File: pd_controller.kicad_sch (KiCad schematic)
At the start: 28 parts, among them Q1 IRF9358TRPBF, Q2 BSL308PEH6327XTSA1, U2 CYPD3177-24LQXQT

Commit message: started routing
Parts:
- TP10, TP11, TP12, TP13: footprint TestPoint:TestPoint_Pad_D2.5mm -> TestPoint:TestPoint_Plated_Hole_D3.0mm
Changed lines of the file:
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@@
 			)
 		)
-		(property "Footprint" "TestPoint:TestPoint_Pad_D2.5mm"
+		(property "Footprint" "TestPoint:TestPoint_Plated_Hole_D3.0mm"
 			(at 93.98 125.73 0)
 			(effects
@@
 			)
 		)
-		(property "Footprint" "TestPoint:TestPoint_Pad_D2.5mm"
+		(property "Footprint" "TestPoint:TestPoint_Plated_Hole_D3.0mm"
 			(at 68.58 125.73 0)
 			(effects
@@
 			)
 		)
-		(property "Footprint" "TestPoint:TestPoint_Pad_D2.5mm"
+		(property "Footprint" "TestPoint:TestPoint_Plated_Hole_D3.0mm"
 			(at 119.38 125.73 0)
 			(effects
@@
 			)
 		)
-		(property "Footprint" "TestPoint:TestPoint_Pad_D2.5mm"
+		(property "Footprint" "TestPoint:TestPoint_Plated_Hole_D3.0mm"
 			(at 48.26 125.73 0)
 			(effects

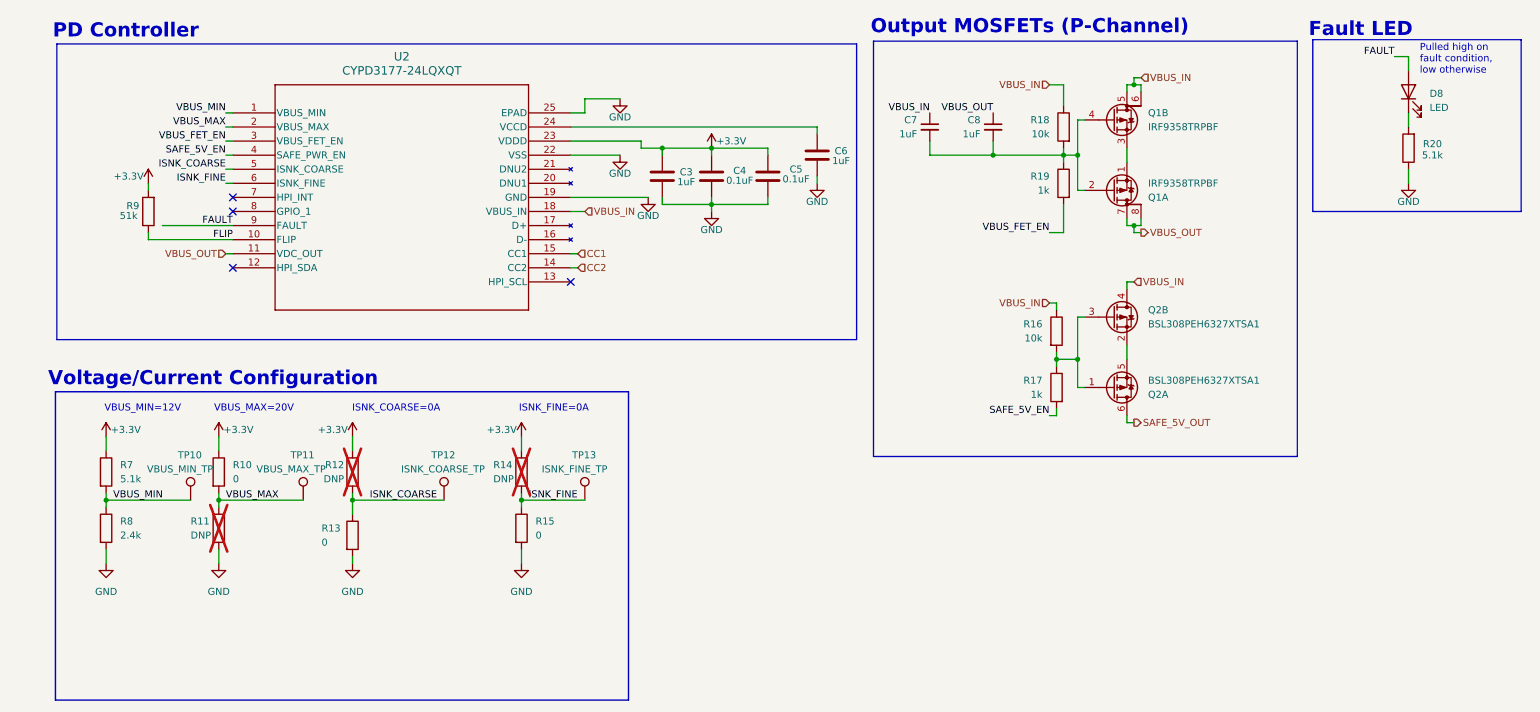
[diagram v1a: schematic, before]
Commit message: redid cypd layout, halfway through 12v buck layout
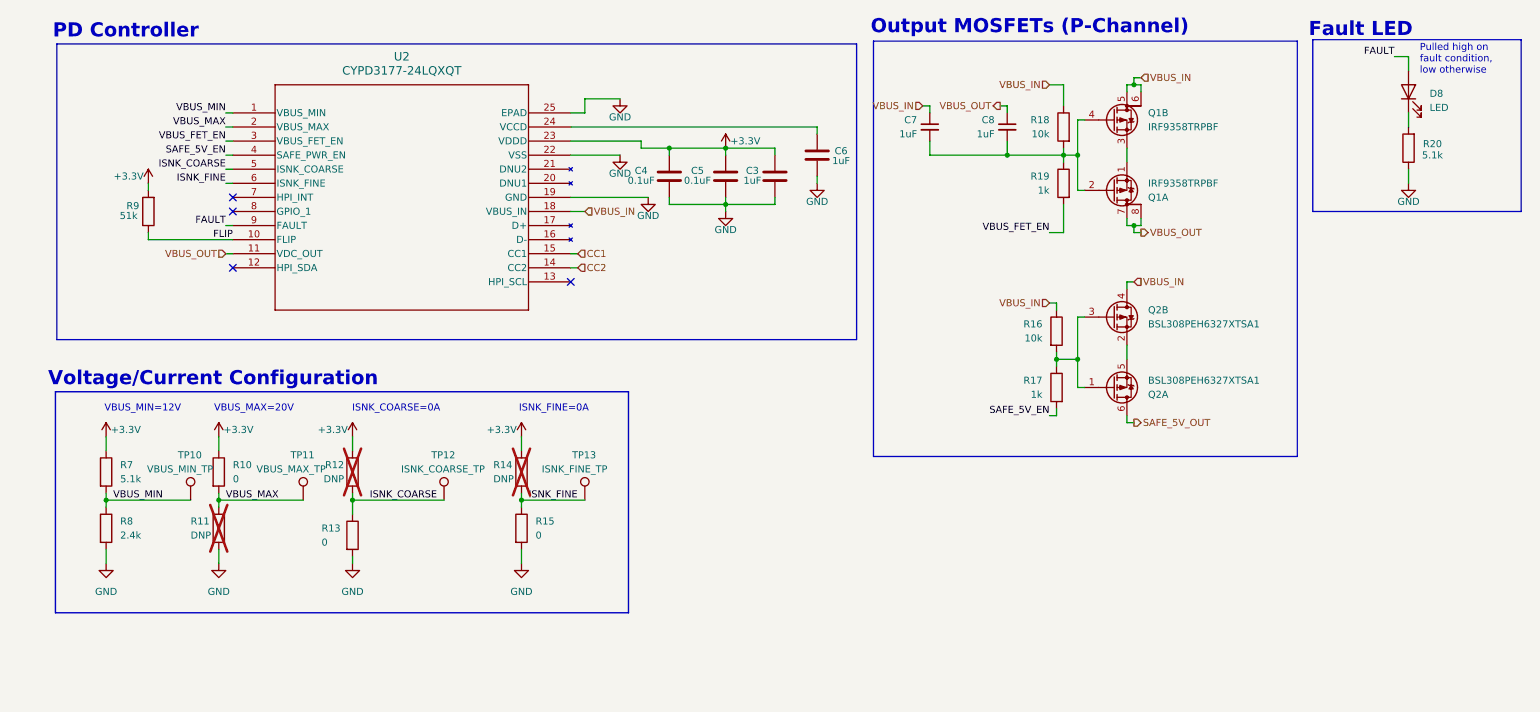
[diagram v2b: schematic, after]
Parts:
- TP10, TP11, TP12, TP13: footprint TestPoint:TestPoint_Plated_Hole_D3.0mm -> TestPoint:TestPoint_THTPad_1.0x1.0mm_Drill0.5mm
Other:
- moved on the sheet: C3, C4, C5, C8

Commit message: addressed some review comments from my 🐐 champers fu
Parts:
- removed TP10: VBUS_MIN_TP, TestPoint:TestPoint_THTPad_1.0x1.0mm_Drill0.5mm, symbol Connector:TestPoint
- removed TP11: VBUS_MAX_TP, TestPoint:TestPoint_THTPad_1.0x1.0mm_Drill0.5mm, symbol Connector:TestPoint
- removed TP12: ISNK_COARSE_TP, TestPoint:TestPoint_THTPad_1.0x1.0mm_Drill0.5mm, symbol Connector:TestPoint
- removed TP13: ISNK_FINE_TP, TestPoint:TestPoint_THTPad_1.0x1.0mm_Drill0.5mm, symbol Connector:TestPoint

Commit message: ready for review 👍🏾
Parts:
- Q1: footprint UTSVT_ICs:SO8_IRF9358TRPBF_INF -> Package_SO:SO-8_3.9x4.9mm_P1.27mm
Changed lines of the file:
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@@
 			)
 		)
-		(property "Footprint" "UTSVT_ICs:SO8_IRF9358TRPBF_INF"
+		(property "Footprint" "Package_SO:SO-8_3.9x4.9mm_P1.27mm"
 			(at 210.82 57.15 0)
 			(effects
@@
 			)
 		)
-		(property "Footprint" "UTSVT_ICs:SO8_IRF9358TRPBF_INF"
+		(property "Footprint" "Package_SO:SO-8_3.9x4.9mm_P1.27mm"
 			(at 210.82 69.85 0)
 			(effects

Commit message: i am jesus christ in the flesh.
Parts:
- C3, C6, C7, C8: Mouser Part Number C0805C105K5PACTU -> (none); P/N (none) -> C0805C105K5PACTU
- C4, C5: Mouser Part Number C0805C104M5RACTU -> (none); P/N (none) -> C0805C104M5RACTU
- D8: Mouser Part Number 604-APTD2012LCGCK -> (none); P/N (none) -> APTD2012LCGCK
- Q1: Mouser Part Number IRF9358TRPBF -> (none); P/N (none) -> IRF9358TRPBF
- Q2: Mouser Part Number BSL308PEH6327XTSA1 -> (none); P/N (none) -> BSL308PEH6327XTSA1
- R16, R18: Mouser Part Number CRCW080510K0FKEAC -> (none); P/N (none) -> CRCW080510K0FKEAC
- R17, R19: Mouser Part Number CRCW08051K00FKEAC -> (none); P/N (none) -> CRCW08051K00FKEAC
- R20, R7: Mouser Part Number CRCW08055K10FKEAC -> (none); P/N (none) -> CRCW08055K10FKEAC
- R8: Mouser Part Number CRCW08052K40FKEAC -> (none); P/N (none) -> CRCW08052K40JNEA
- R9: Mouser Part Number CRCW080551K0FKEAC -> (none); P/N (none) -> CRCW080551K0FKEAC
- U2: Mouser Part Number 727-CYPD3177-24LQXQT -> (none); P/N (none) -> CYPD3177-24LQXQT
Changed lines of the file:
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@@
 			)
 		)
-		(property "Mouser Part Number" "BSL308PEH6327XTSA1"
+		(property "Mouser Part Number" ""
+			(at 209.55 105.41 0)
+			(effects
+				(font
+					(size 1.27 1.27)
+				)
+				(hide yes)
+			)
+		)
+		(property "P/N" "BSL308PEH6327XTSA1"
 			(at 209.55 105.41 0)
 			(effects
@@
 			)
 		)
-		(property "Mouser Part Number" "CRCW080510K0FKEAC "
+		(property "Mouser Part Number" ""
 			(at 200.66 58.42 0)
 			(effects
@@
 			)
 		)
+		(property "P/N" "CRCW080510K0FKEAC"
+			(at 200.66 58.42 0)
+			(effects
+				(font
+					(size 1.27 1.27)
+				)
+				(hide yes)
+			)
+		)
 		(pin "1"
 		)
@@
 			)
 		)
-		(property "Mouser Part Number" "727-CYPD3177-24LQXQT"
+		(property "Mouser Part Number" ""
 			(at 50.8 55.88 0)
 			(effects
@@
 			)
 		)
+		(property "P/N" "CYPD3177-24LQXQT"
+			(at 50.8 55.88 0)
+			(effects
+				(font
+					(size 1.27 1.27)
+				)
+				(hide yes)
+			)
+		)
 		(pin "1"
 		)
@@
 			)
 		)
-		(property "Mouser Part Number" "BSL308PEH6327XTSA1"
+		(property "Mouser Part Number" ""
+			(at 209.55 92.71 0)
+			(effects
+				(font
+					(size 1.27 1.27)
+				)
+				(hide yes)
+			)
+		)
+		(property "P/N" "BSL308PEH6327XTSA1"
 			(at 209.55 92.71 0)
 			(effects
@@
 			)
 		)
-		(property "Mouser Part Number" "604-APTD2012LCGCK"
+		(property "Mouser Part Number" ""
 			(at 262.89 52.07 0)
 			(effects
@@
 			)
 		)
+		(property "P/N" "APTD2012LCGCK"
+			(at 262.89 52.07 0)
+			(effects
+				(font
+					(size 1.27 1.27)
+				)
+				(hide yes)
+			)
+		)
 		(pin "2"
 		)
@@
 			)
 		)
-		(property "Mouser Part Number" "C0805C105K5PACTU"
+		(property "Mouser Part Number" ""
 			(at 176.53 58.42 0)
 			(effects
@@
 			)
 		)
+		(property "P/N" "C0805C105K5PACTU"
+			(at 176.53 58.42 0)
+			(effects
+				(font
+					(size 1.27 1.27)
+				)
+				(hide yes)
+			)
+		)
 		(pin "1"
 		)
@@
 			)
 		)
-		(property "Mouser Part Number" "C0805C105K5PACTU"
+		(property "Mouser Part Number" ""
 			(at 156.21 63.5 0)
 			(effects
@@
 			)
 		)
+		(property "P/N" "C0805C105K5PACTU"
+			(at 156.21 63.5 0)
+			(effects
+				(font
+					(size 1.27 1.27)
+				)
+				(hide yes)
+			)
+		)
 		(pin "1"
 		)
@@
 			)
 		)
-		(property "Mouser Part Number" "C0805C105K5PACTU"
+		(property "Mouser Part Number" ""
 			(at 148.59 67.31 0)
 			(effects
@@
 			)
 		)
+		(property "P/N" "C0805C105K5PACTU"
+			(at 148.59 67.31 0)
+			(effects
+				(font
+					(size 1.27 1.27)
+				)
+				(hide yes)
+			)
+		)
 		(pin "1"
 		)
@@
 			)
 		)
-		(property "Mouser Part Number" "CRCW08052K40FKEAC"
+		(property "Mouser Part Number" ""
 			(at 27.94 130.81 0)
 			(effects
@@
 			)
 		)
+		(property "P/N" "CRCW08052K40JNEA"
+			(at 27.94 130.81 0)
+			(effects
+				(font
+					(size 1.27 1.27)
+				)
+				(hide yes)
+			)
+		)
 		(pin "2"
 		)
@@
 			)
 		)
-		(property "Mouser Part Number" "CRCW08055K10FKEAC "
+		(property "Mouser Part Number" ""
 			(at 27.94 120.65 0)
 			(effects
@@
 			)
 		)
+		(property "P/N" "CRCW08055K10FKEAC "
+			(at 27.94 120.65 0)
+			(effects
+				(font
+					(size 1.27 1.27)
+				)
+				(hide yes)
+			)
+		)
 		(pin "2"
 		)
@@
 			)
 		)
-		(property "Mouser Part Number" "CRCW080510K0FKEAC "
+		(property "Mouser Part Number" ""
 			(at 199.39 95.25 0)
 			(effects
@@
 			)
 		)
+		(property "P/N" "CRCW080510K0FKEAC"
+			(at 199.39 95.25 0)
+			(effects
+				(font
+					(size 1.27 1.27)
+				)
+				(hide yes)
+			)
+		)
 		(pin "1"
 		)
@@
 			)
 		)
-		(property "Mouser Part Number" "C0805C105K5PACTU"
+		(property "Mouser Part Number" ""
 			(at 190.5 58.42 0)
 			(effects
@@
 			)
 		)
+		(property "P/N" "C0805C105K5PACTU"
+			(at 190.5 58.42 0)
+			(effects
+				(font
+					(size 1.27 1.27)
+				)
+				(hide yes)
+			)
+		)
 		(pin "1"
 		)
@@
 			)
 		)
-		(property "Mouser Part Number" "IRF9358TRPBF"
+		(property "Mouser Part Number" ""
+			(at 209.55 57.15 0)
+			(effects
+				(font
+					(size 1.27 1.27)
+				)
+				(hide yes)
+			)
+		)
+		(property "P/N" "IRF9358TRPBF"
 			(at 209.55 57.15 0)
 			(effects
@@
 			)
 		)
-		(property "Mouser Part Number" "C0805C104M5RACTU"
+		(property "Mouser Part Number" ""
 			(at 139.7 67.31 0)
 			(effects
@@
 			)
 		)
+		(property "P/N" "C0805C104M5RACTU"
+			(at 139.7 67.31 0)
+			(effects
+				(font
+					(size 1.27 1.27)
+				)
+				(hide yes)
+			)
+		)
 		(pin "1"
 		)
@@
 			)
 		)
-		(property "Mouser Part Number" "C0805C104M5RACTU"
+		(property "Mouser Part Number" ""
 			(at 129.54 67.31 0)
 			(effects
@@
 			)
 		)
+		(property "P/N" "C0805C104M5RACTU"
+			(at 129.54 67.31 0)
+			(effects
+				(font
+					(size 1.27 1.27)
+				)
+				(hide yes)
+			)
+		)
 		(pin "1"
 		)
@@
 			)
 		)
-		(property "Mouser Part Number" "CRCW08051K00FKEAC"
+		(property "Mouser Part Number" ""
 			(at 200.66 68.58 0)
 			(effects
@@
 			)
 		)
+		(property "P/N" "CRCW08051K00FKEAC"
+			(at 200.66 68.58 0)
+			(effects
+				(font
+					(size 1.27 1.27)
+				)
+				(hide yes)
+			)
+		)
 		(pin "1"
 		)
@@
 			)
 		)
-		(property "Mouser Part Number" "CRCW08051K00FKEAC"
+		(property "Mouser Part Number" ""
 			(at 199.39 105.41 0)
 			(effects
@@
 			)
 		)
+		(property "P/N" "CRCW08051K00FKEAC"
+			(at 199.39 105.41 0)
+			(effects
+				(font
+					(size 1.27 1.27)
+				)
+				(hide yes)
+			)
+		)
 		(pin "1"
 		)
@@
 			)
 		)
-		(property "Mouser Part Number" "CRCW080551K0FKEAC"
+		(property "Mouser Part Number" ""
 			(at 35.56 73.66 0)
 			(effects
@@
 			)
 		)
+		(property "P/N" "CRCW080551K0FKEAC"
+			(at 35.56 73.66 0)
+			(effects
+				(font
+					(size 1.27 1.27)
+				)
+				(hide yes)
+			)
+		)
 		(pin "2"
 		)
@@
 			)
 		)
-		(property "Mouser Part Number" "CRCW08055K10FKEAC "
+		(property "Mouser Part Number" ""
 			(at 262.89 62.23 0)
 			(effects
@@
 			)
 		)
+		(property "P/N" "CRCW08055K10FKEAC "
+			(at 262.89 62.23 0)
+			(effects
+				(font
+					(size 1.27 1.27)
+				)
+				(hide yes)
+			)
+		)
 		(pin "2"
 		)
@@
 			)
 		)
-		(property "Mouser Part Number" "IRF9358TRPBF"
+		(property "Mouser Part Number" ""
+			(at 209.55 69.85 0)
+			(effects
+				(font
+					(size 1.27 1.27)
+				)
+				(hide yes)
+			)
+		)
+		(property "P/N" "IRF9358TRPBF"
 			(at 209.55 69.85 0)
 			(effects
